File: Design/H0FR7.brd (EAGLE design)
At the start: 60 x 34.6 mm, 46 parts, among them P1 HEXABIT_X2_P1_P5_EDIT_POWER_P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, Q1 MMBT3904LT1, Q2 STD36P4LLF6, U1 STM32G0B1CEU6QFN_B1CEU6_STM-L, U2 TSV772IYDT, U3 PMD3001D,115, X1 XTALL_CSTCE8M00G52

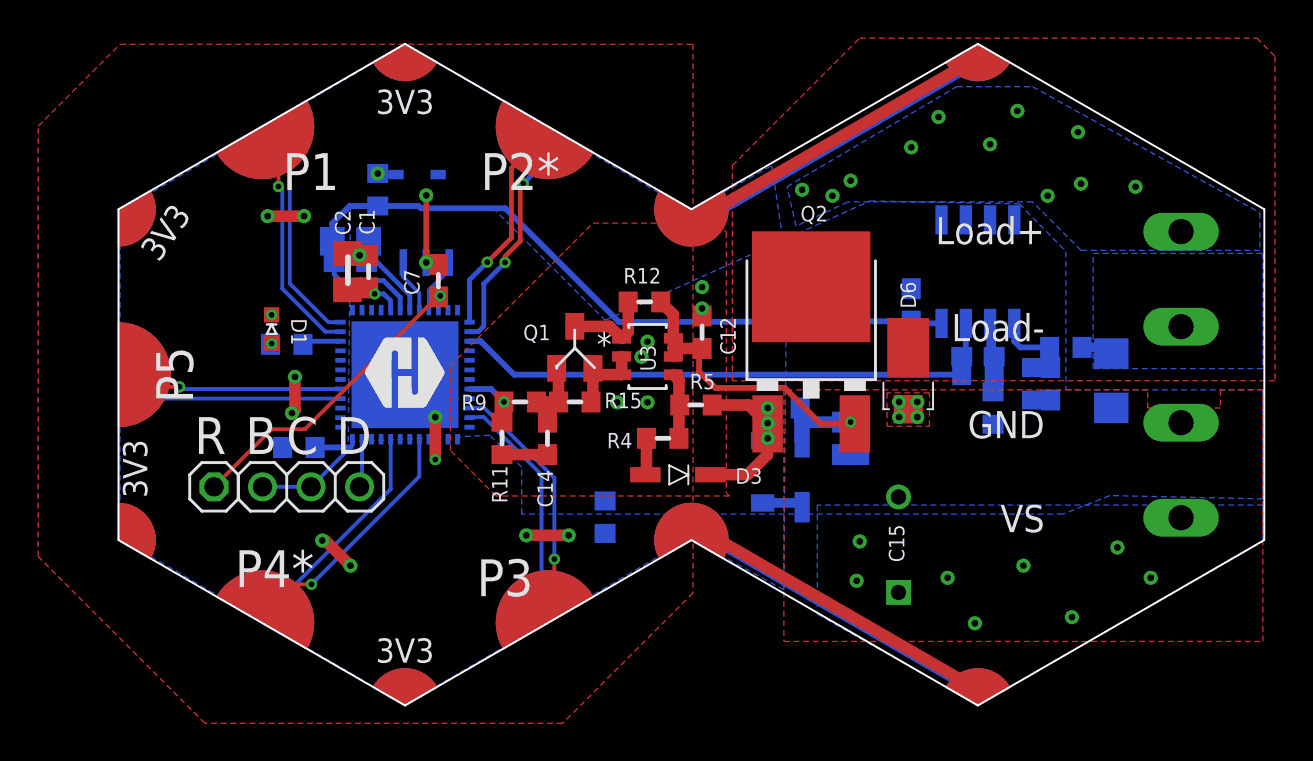
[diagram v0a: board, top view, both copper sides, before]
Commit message: -Activate the thermal option for the polygon
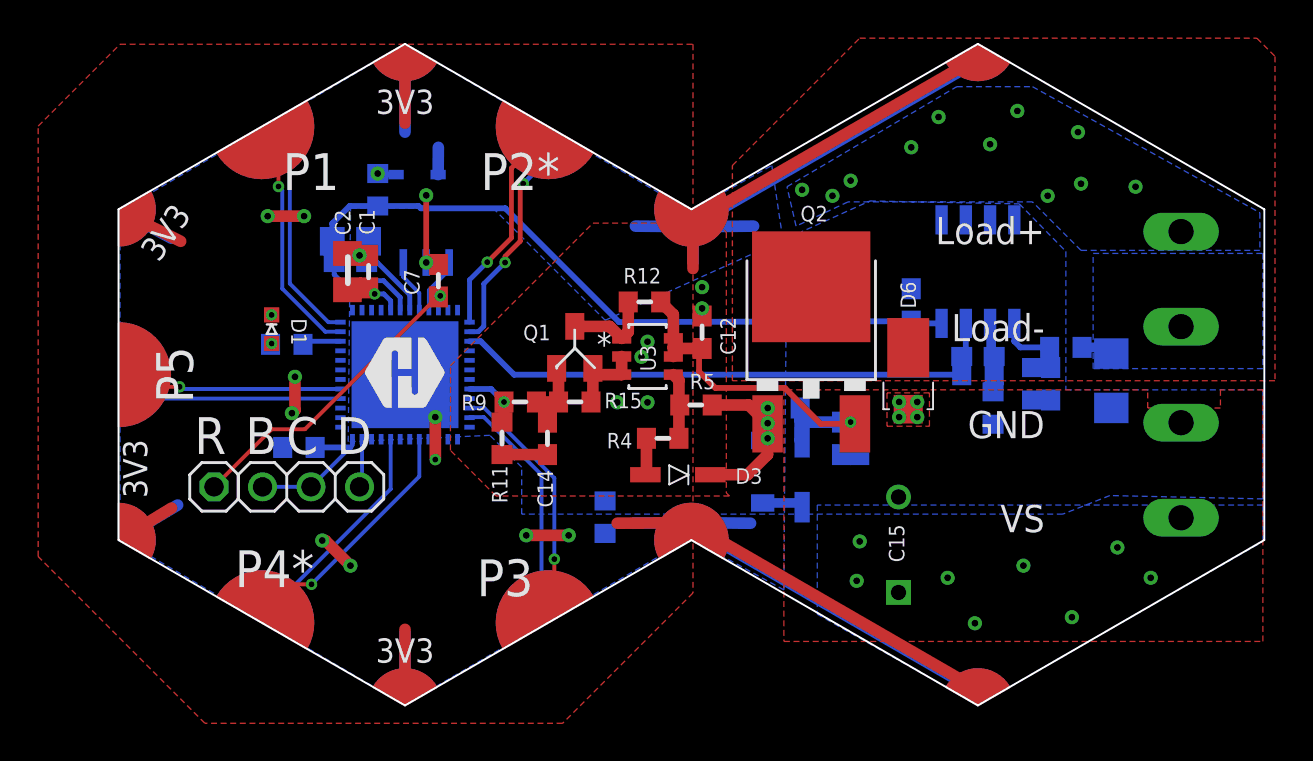
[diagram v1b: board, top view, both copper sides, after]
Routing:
- net GND: track 52.2 -> 79.9 mm
- net VDD: track 36.0 -> 53.9 mm
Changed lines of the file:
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@@
 <drawing>
 <settings>
-<setting alwaysvectorfont="yes"/>
+<setting alwaysvectorfont="no"/>
 <setting verticaltext="up"/>
 </settings>
@@
 <wire x1="-0.1421375" y1="16.98324375" x2="-0.14514375" y2="16.98625" width="0.6096" layer="16"/>
 <wire x1="-0.14514375" y1="16.98625" x2="-0.15875" y2="16.98625" width="0.6096" layer="16"/>
-<polygon width="0.1524" layer="16" thermals="no" rank="2">
+<polygon width="0.1524" layer="16" rank="2">
 <vertex x="4.797971875" y="2.814559375"/>
 <vertex x="4.7625" y="-2.54"/>
@@
 <wire x1="-15.08125" y1="8.73125" x2="-13.49375" y2="7.14375" width="0.6096" layer="16"/>
 <wire x1="-13.49375" y1="7.14375" x2="-13.49375" y2="6.50875" width="0.6096" layer="16"/>
+<wire x1="-29.3879875" y1="16.99125" x2="-27.305" y2="15.875" width="0.6096" layer="16"/>
+<wire x1="-29.3879875" y1="0.471253125" x2="-26.9875" y2="1.905" width="0.6096" layer="16"/>
+<wire x1="-15.08125" y1="-7.78875" x2="-15.08125" y2="-4.7625" width="0.6096" layer="16"/>
+<wire x1="-0.00925" y1="0.97925" x2="-3.175" y2="0.9525" width="0.6096" layer="16"/>
+<wire x1="-0.00925" y1="0.97925" x2="3.01625" y2="0.9525" width="0.6096" layer="16"/>
+<wire x1="-0.00925" y1="16.48325" x2="0" y2="14.605" width="0.6096" layer="16"/>
+<wire x1="-0.00925" y1="16.48325" x2="-3.01625" y2="16.51" width="0.6096" layer="16"/>
+<wire x1="-0.00925" y1="16.48325" x2="3.175" y2="16.51" width="0.6096" layer="16"/>
+<wire x1="-15.08125" y1="25.25125" x2="-15.08125" y2="21.43125" width="0.6096" layer="16"/>
+<wire x1="-13.34625" y1="19.20875" x2="-13.335" y2="20.6375" width="0.6096" layer="16"/>
 </signal>
 <signal name="VDD">
@@
 <wire x1="14.91875" y1="-7.78875" x2="14.835846875" y2="-7.705846875" width="0.6096" layer="1"/>
 <wire x1="14.835846875" y1="-7.705846875" x2="0.7477375" y2="0.4276875" width="0.6096" layer="1"/>
-<polygon width="0.1524" layer="1" thermals="no" rank="2">
+<polygon width="0.1524" layer="1" rank="2">
 <vertex x="0" y="26.035"/>
 <vertex x="0" y="-2.69875"/>
@@
 <wire x1="0.7477375" y1="0.4276875" x2="0.811675" y2="0.36375" width="0.508" layer="1"/>
 <wire x1="0.811675" y1="0.36375" x2="0.60625" y2="0.36375" width="0.508" layer="1"/>
+<wire x1="-15.08125" y1="-7.78875" x2="-15.08125" y2="-4.60375" width="0.6096" layer="1"/>
+<wire x1="-29.3879875" y1="0.471253125" x2="-27.305" y2="1.74625" width="0.6096" layer="1"/>
+<wire x1="-29.3879875" y1="16.99125" x2="-26.82875" y2="15.71625" width="0.6096" layer="1"/>
+<wire x1="-15.08125" y1="25.25125" x2="-15.08125" y2="21.9075" width="0.6096" layer="1"/>
+<wire x1="-0.00925" y1="16.48325" x2="0" y2="14.2875" width="0.6096" layer="1"/>
+<wire x1="-0.00925" y1="0.97925" x2="-3.96875" y2="0.9525" width="0.6096" layer="1"/>
+<wire x1="-0.00925" y1="0.97925" x2="0" y2="14.2875" width="0" layer="19" extent="1-1"/>
 </signal>
 <signal name="UART3_TX">
